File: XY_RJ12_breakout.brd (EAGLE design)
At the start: 57 x 79 mm, 36 parts

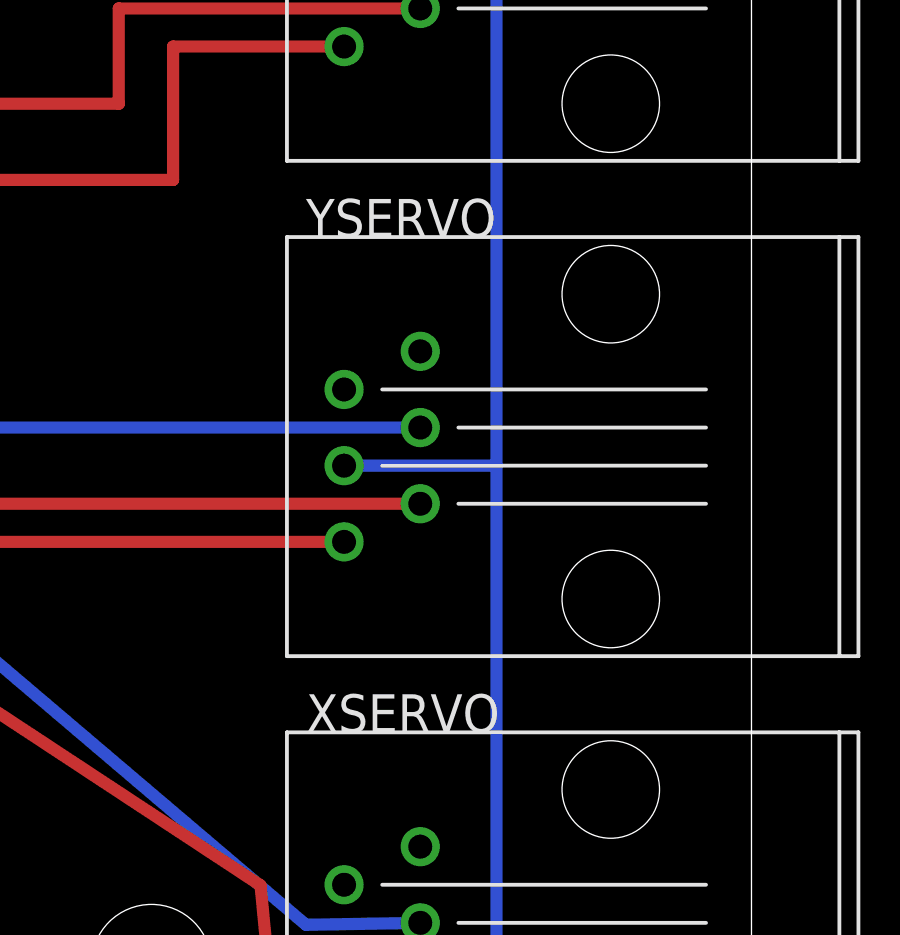
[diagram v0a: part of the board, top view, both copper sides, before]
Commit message: Fix wrong label on XSTEPPER and YSTEPPER port
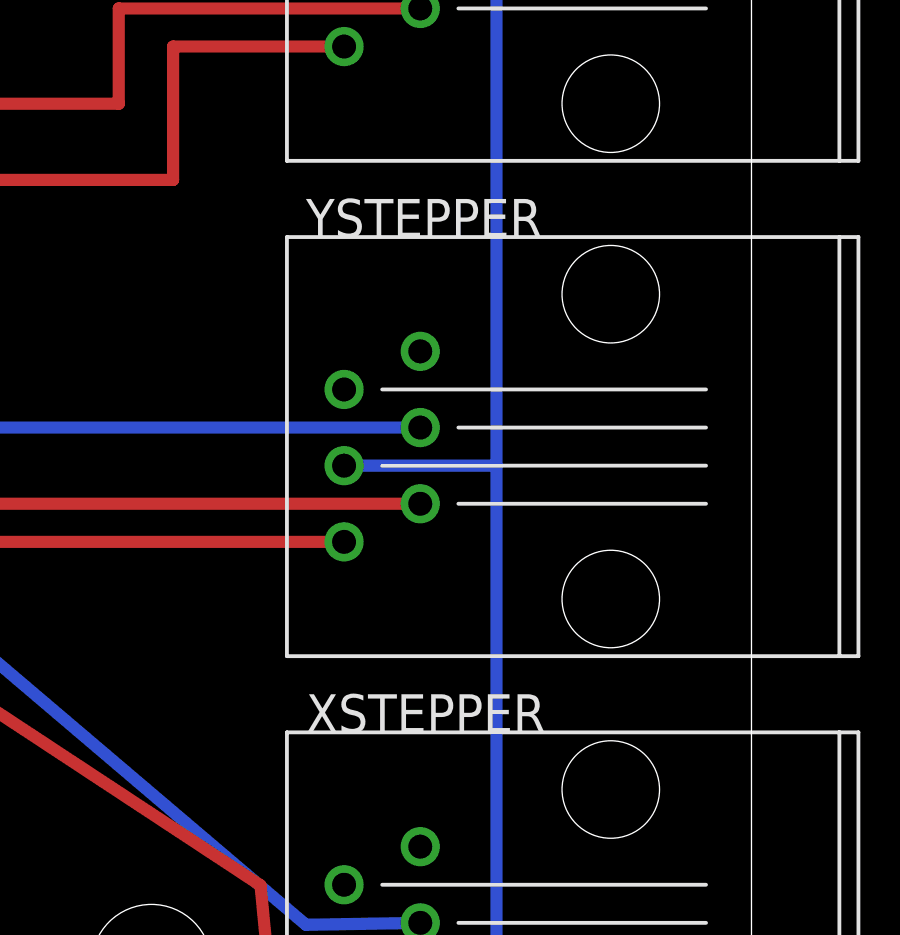
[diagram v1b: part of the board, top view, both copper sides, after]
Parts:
- renumbered XSERVO to XSTEPPER, YSERVO to YSTEPPER
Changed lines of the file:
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@@
 <?xml version="1.0" encoding="utf-8"?>
 <!DOCTYPE eagle SYSTEM "eagle.dtd">
-<eagle version="7.3.0">
+<eagle version="7.6.0">
 <drawing>
 <settings>
@@
 <element name="SERVO" library="con-rj" package="RJ12" value="RJ12" x="31.75" y="92.71" rot="R90"/>
 <element name="XLIMIT" library="con-rj" package="RJ12" value="RJ12" x="67.31" y="64.77"/>
-<element name="XSERVO" library="con-rj" package="RJ12" value="RJ12" x="67.31" y="31.75"/>
+<element name="XSTEPPER" library="con-rj" package="RJ12" value="RJ12" x="67.31" y="31.75"/>
 <element name="YLIMIT" library="con-rj" package="RJ12" value="RJ12" x="48.26" y="92.71" rot="R90"/>
-<element name="YSERVO" library="con-rj" package="RJ12" value="RJ12" x="67.31" y="48.26"/>
+<element name="YSTEPPER" library="con-rj" package="RJ12" value="RJ12" x="67.31" y="48.26"/>
 <element name="JP1" library="pinhead" package="1X01" value="" x="24.13" y="77.47"/>
 <element name="JP2" library="pinhead" package="1X01" value="" x="24.13" y="74.93"/>
@@
 <wire x1="63.5" y1="47.625" x2="63.5" y2="65.405" width="0.4064" layer="16"/>
 <wire x1="24.13" y1="77.47" x2="19.05" y2="77.47" width="0.4064" layer="16"/>
-<contactref element="YSERVO" pad="3"/>
-<contactref element="XSERVO" pad="3"/>
+<contactref element="YSTEPPER" pad="3"/>
+<contactref element="XSTEPPER" pad="3"/>
 <wire x1="58.42" y1="31.115" x2="63.5" y2="31.115" width="0.4064" layer="16"/>
 <wire x1="58.42" y1="47.625" x2="63.5" y2="47.625" width="0.4064" layer="16"/>
@@
 <wire x1="44.45" y1="48.895" x2="44.45" y2="43.115" width="0.4064" layer="16"/>
 <wire x1="24.13" y1="72.39" x2="19.05" y2="72.39" width="0.4064" layer="16"/>
-<contactref element="XSERVO" pad="4"/>
+<contactref element="XSTEPPER" pad="4"/>
 <wire x1="44.45" y1="43.115" x2="57.15" y2="32.32" width="0.4064" layer="16"/>
 <wire x1="57.15" y1="32.32" x2="60.96" y2="32.385" width="0.4064" layer="16"/>
-<contactref element="YSERVO" pad="4"/>
+<contactref element="YSTEPPER" pad="4"/>
 <wire x1="60.96" y1="48.895" x2="44.45" y2="48.895" width="0.4064" layer="16"/>
 </signal>
@@
 <signal name="N$10">
 <contactref element="J6" pad="11"/>
-<contactref element="YSERVO" pad="2"/>
+<contactref element="YSTEPPER" pad="2"/>
 <wire x1="24.13" y1="54.61" x2="30.48" y2="54.61" width="0.4064" layer="1"/>
 <wire x1="30.48" y1="54.61" x2="45.72" y2="54.61" width="0.4064" layer="1"/>
@@
 <signal name="N$11">
 <contactref element="J6" pad="10"/>
-<contactref element="YSERVO" pad="1"/>
+<contactref element="YSTEPPER" pad="1"/>
 <wire x1="24.13" y1="52.07" x2="30.48" y2="52.07" width="0.4064" layer="1"/>
 <wire x1="30.48" y1="52.07" x2="43.18" y2="52.07" width="0.4064" layer="1"/>
@@
 <signal name="N$12">
 <contactref element="J6" pad="9"/>
-<contactref element="XSERVO" pad="2"/>
+<contactref element="XSTEPPER" pad="2"/>
 <wire x1="24.13" y1="49.53" x2="30.48" y2="49.53" width="0.4064" layer="1"/>
 <wire x1="30.48" y1="49.53" x2="41.64" y2="49.53" width="0.4064" layer="1"/>
@@
 <signal name="N$13">
 <contactref element="J6" pad="8"/>
-<contactref element="XSERVO" pad="1"/>
+<contactref element="XSTEPPER" pad="1"/>
 <wire x1="24.13" y1="46.99" x2="30.48" y2="46.99" width="0.4064" layer="1"/>
 <wire x1="30.48" y1="46.99" x2="40.1" y2="46.99" width="0.4064" layer="1"/>
